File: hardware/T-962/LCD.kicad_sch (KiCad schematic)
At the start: 9 parts

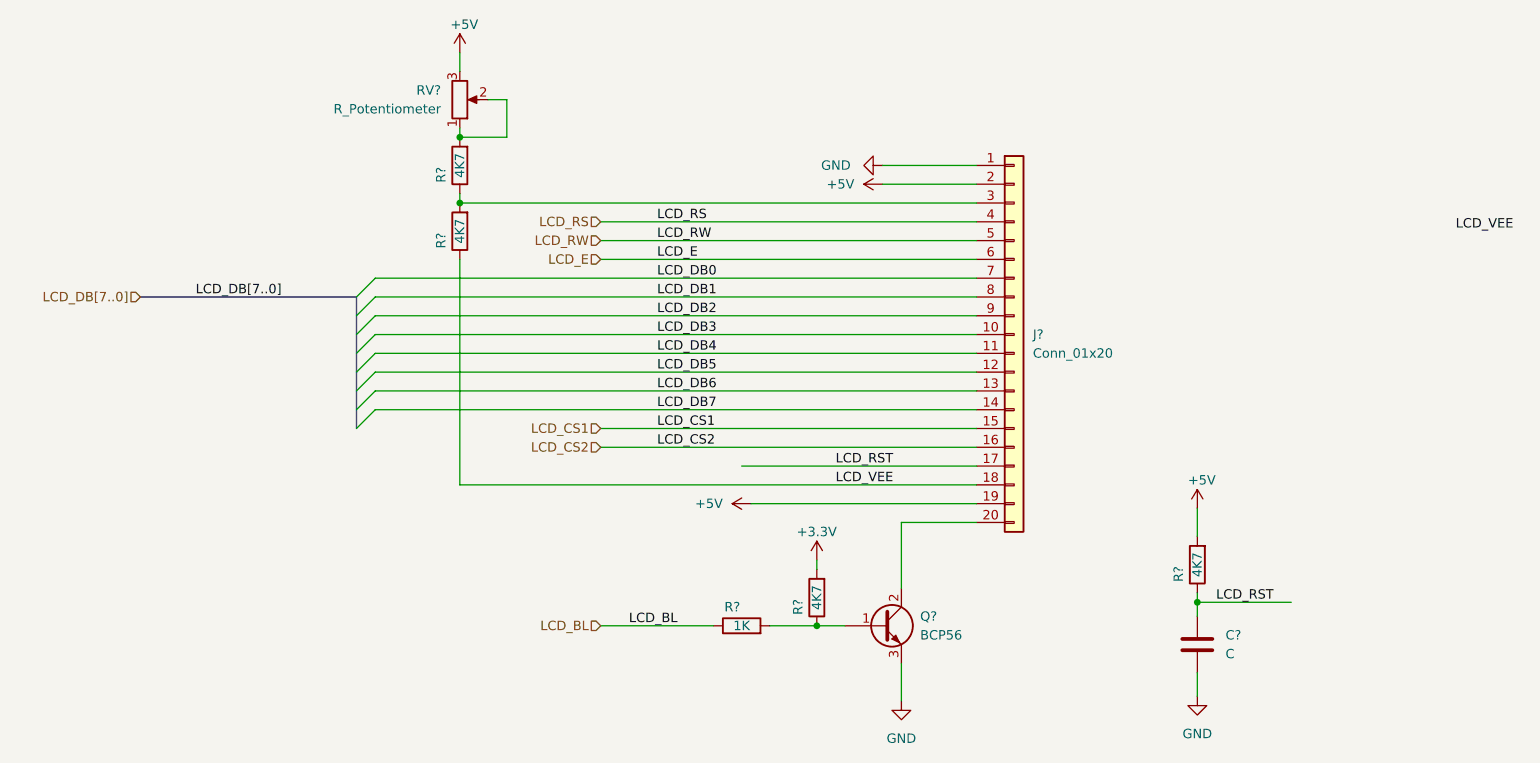
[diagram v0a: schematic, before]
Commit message: add max31850 thermocouple interfaces
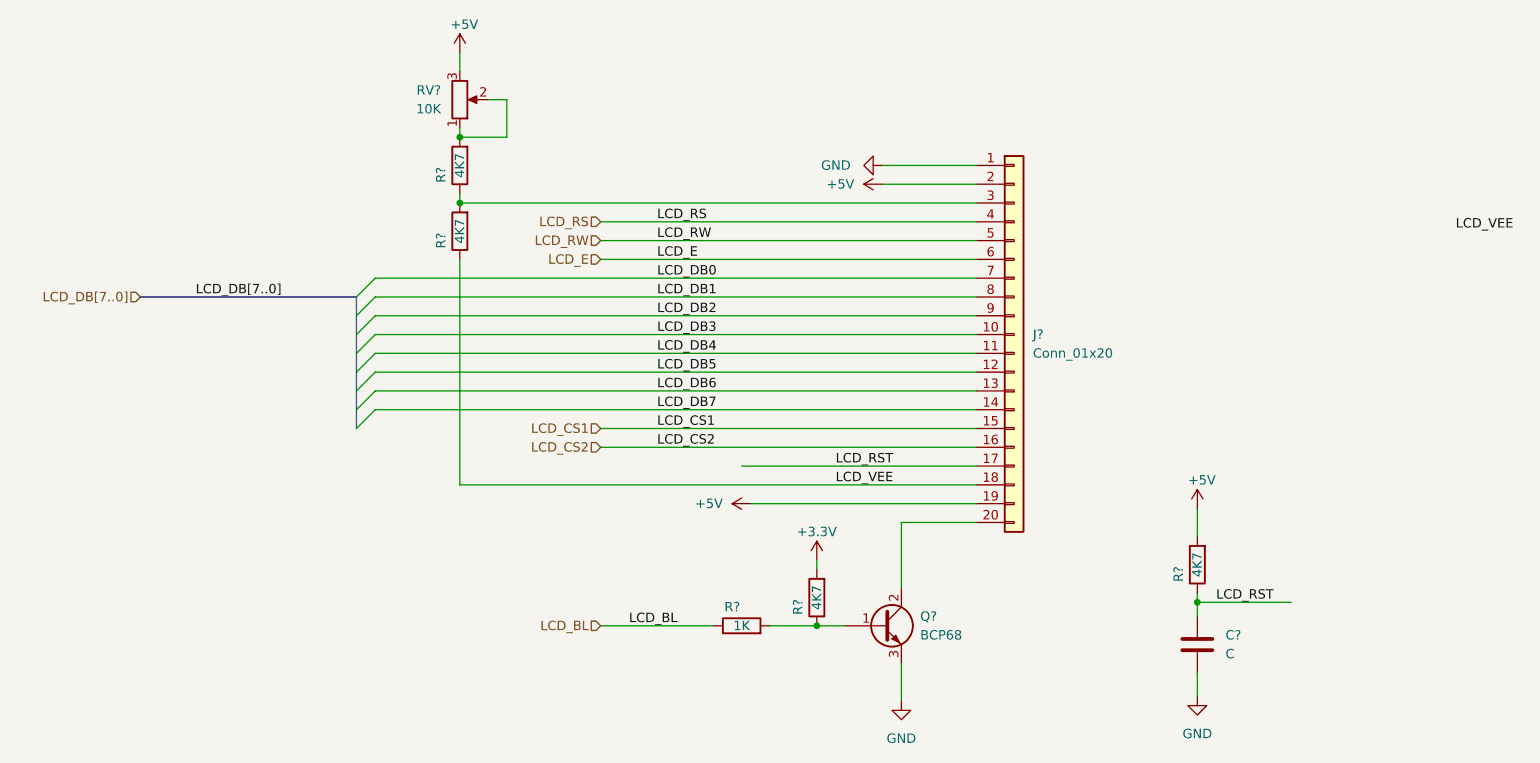
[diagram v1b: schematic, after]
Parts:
- Q?: value BCP56 -> BCP68
- RV?: value R_Potentiometer -> 10K
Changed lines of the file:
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@@
       (effects (font (size 1.27 1.27)) (justify right))
     )
-    (property "Value" "R_Potentiometer" (id 1) (at 92.71 59.6899 0)
+    (property "Value" "10K" (id 1) (at 92.71 59.6899 0)
       (effects (font (size 1.27 1.27)) (justify right))
     )
@@
       (effects (font (size 1.27 1.27)) (justify left))
     )
-    (property "Value" "BCP56" (id 1) (at 157.48 130.8099 0)
+    (property "Value" "BCP68" (id 1) (at 157.48 130.8099 0)
       (effects (font (size 1.27 1.27)) (justify left))
     )

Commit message: fill out designators
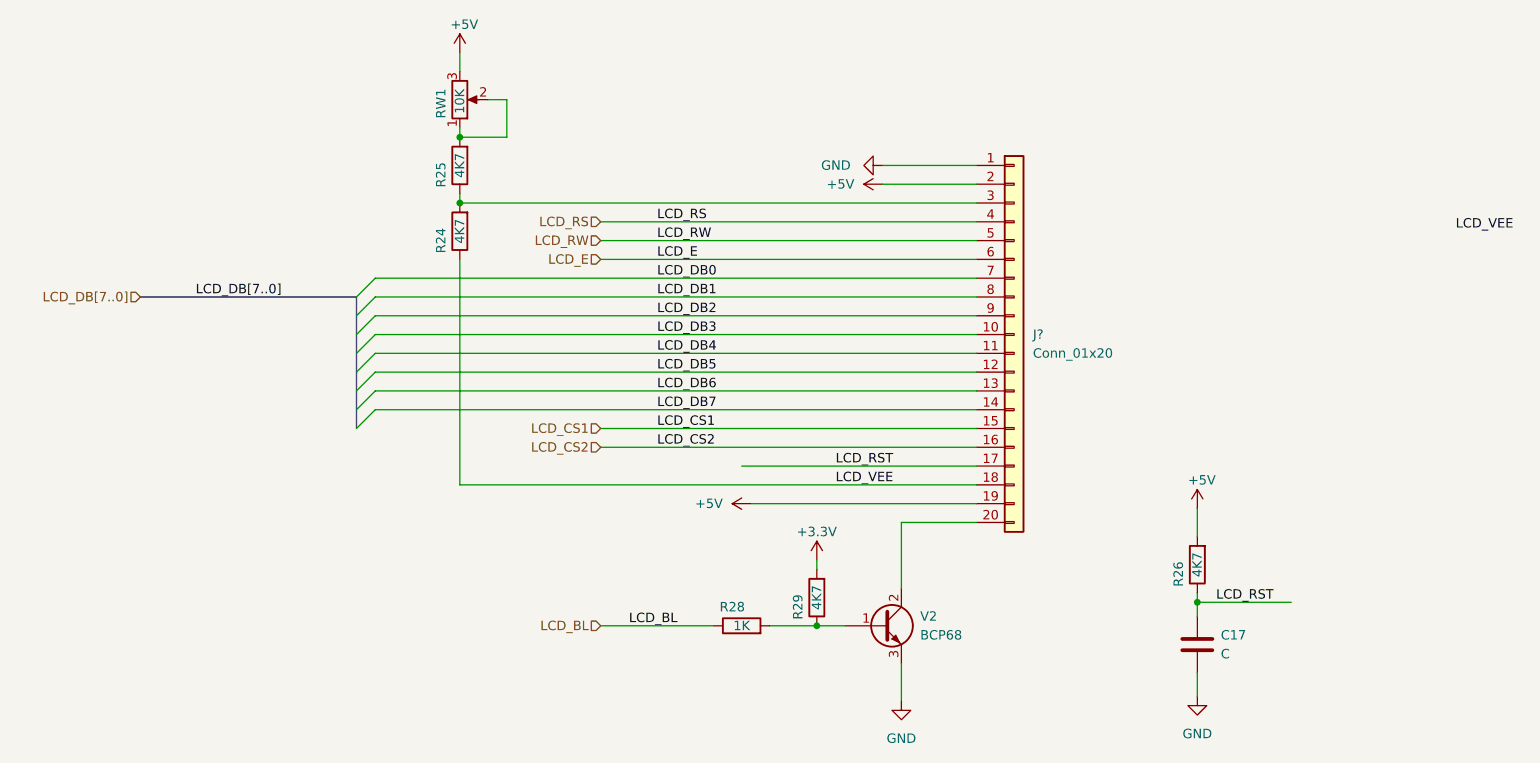
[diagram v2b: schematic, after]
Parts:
- gave numbers to parts that had none: 8
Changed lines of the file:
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@@
   )
   (symbol (lib_id "Device:R_Potentiometer") (at 95.25 58.42 0) (mirror x) (unit 1)
-    (in_bom yes) (on_board yes) (fields_autoplaced)
-    (property "Reference" "RV?" (id 0) (at 92.71 57.1499 0)
+    (in_bom yes) (on_board yes)
+    (property "Reference" "RW1" (id 0) (at 92.71 60.96 90)
       (effects (font (size 1.27 1.27)) (justify right))
     )
-    (property "Value" "10K" (id 1) (at 92.71 59.6899 0)
+    (property "Value" "10K" (id 1) (at 95.25 60.325 90)
       (effects (font (size 1.27 1.27)) (justify right))
     )
@@
   (symbol (lib_id "Transistor_BJT:BCP56") (at 152.4 129.54 0) (unit 1)
     (in_bom yes) (on_board yes) (fields_autoplaced)
-    (property "Reference" "Q?" (id 0) (at 157.48 128.2699 0)
+    (property "Reference" "V2" (id 0) (at 157.48 128.2699 0)
       (effects (font (size 1.27 1.27)) (justify left))
     )
@@
   (symbol (lib_id "Device:R") (at 95.25 76.2 180) (unit 1)
     (in_bom yes) (on_board yes)
-    (property "Reference" "R?" (id 0) (at 92.71 77.47 90))
+    (property "Reference" "R24" (id 0) (at 92.71 77.47 90))
     (property "Value" "4K7" (id 1) (at 95.25 76.2 90))
     (property "Footprint" "" (id 2) (at 97.028 76.2 90)
@@
   (symbol (lib_id "Device:R") (at 143.51 125.73 180) (unit 1)
     (in_bom yes) (on_board yes)
-    (property "Reference" "R?" (id 0) (at 140.97 127 90))
+    (property "Reference" "R29" (id 0) (at 140.97 127 90))
     (property "Value" "4K7" (id 1) (at 143.51 125.73 90))
     (property "Footprint" "" (id 2) (at 145.288 125.73 90)
@@
   (symbol (lib_id "Device:C") (at 194.945 132.08 0) (unit 1)
     (in_bom yes) (on_board yes) (fields_autoplaced)
-    (property "Reference" "C?" (id 0) (at 198.755 130.8099 0)
-      (effects (font (size 1.27 1.27)) (justify left))
-    )
-    (property "Value" "C" (id 1) (at 198.755 133.3499 0)
+    (property "Reference" "C17" (id 0) (at 198.12 130.8099 0)
+      (effects (font (size 1.27 1.27)) (justify left))
+    )
+    (property "Value" "C" (id 1) (at 198.12 133.3499 0)
       (effects (font (size 1.27 1.27)) (justify left))
     )
@@
   (symbol (lib_id "Device:R") (at 194.945 121.285 180) (unit 1)
     (in_bom yes) (on_board yes)
-    (property "Reference" "R?" (id 0) (at 192.405 122.555 90))
+    (property "Reference" "R26" (id 0) (at 192.405 122.555 90))
     (property "Value" "4K7" (id 1) (at 194.945 121.285 90))
     (property "Footprint" "" (id 2) (at 196.723 121.285 90)
@@
   (symbol (lib_id "Device:R") (at 133.35 129.54 90) (unit 1)
     (in_bom yes) (on_board yes)
-    (property "Reference" "R?" (id 0) (at 132.08 127 90))
+    (property "Reference" "R28" (id 0) (at 132.08 127 90))
     (property "Value" "1K" (id 1) (at 133.35 129.54 90))
     (property "Footprint" "" (id 2) (at 133.35 131.318 90)
@@
   (symbol (lib_id "Device:R") (at 95.25 67.31 180) (unit 1)
     (in_bom yes) (on_board yes)
-    (property "Reference" "R?" (id 0) (at 92.71 68.58 90))
+    (property "Reference" "R25" (id 0) (at 92.71 68.58 90))
     (property "Value" "4K7" (id 1) (at 95.25 67.31 90))
     (property "Footprint" "" (id 2) (at 97.028 67.31 90)
